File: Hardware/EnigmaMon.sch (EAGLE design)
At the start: 57 parts, among them IC1 4051N, IC2 TLC5940, IC3 MEGA8-P, T1 BC548, T2 BC548, T3 BC548, T4 BC548, T5 BC548, T6 BC548, T8 BC548, T9 BC548

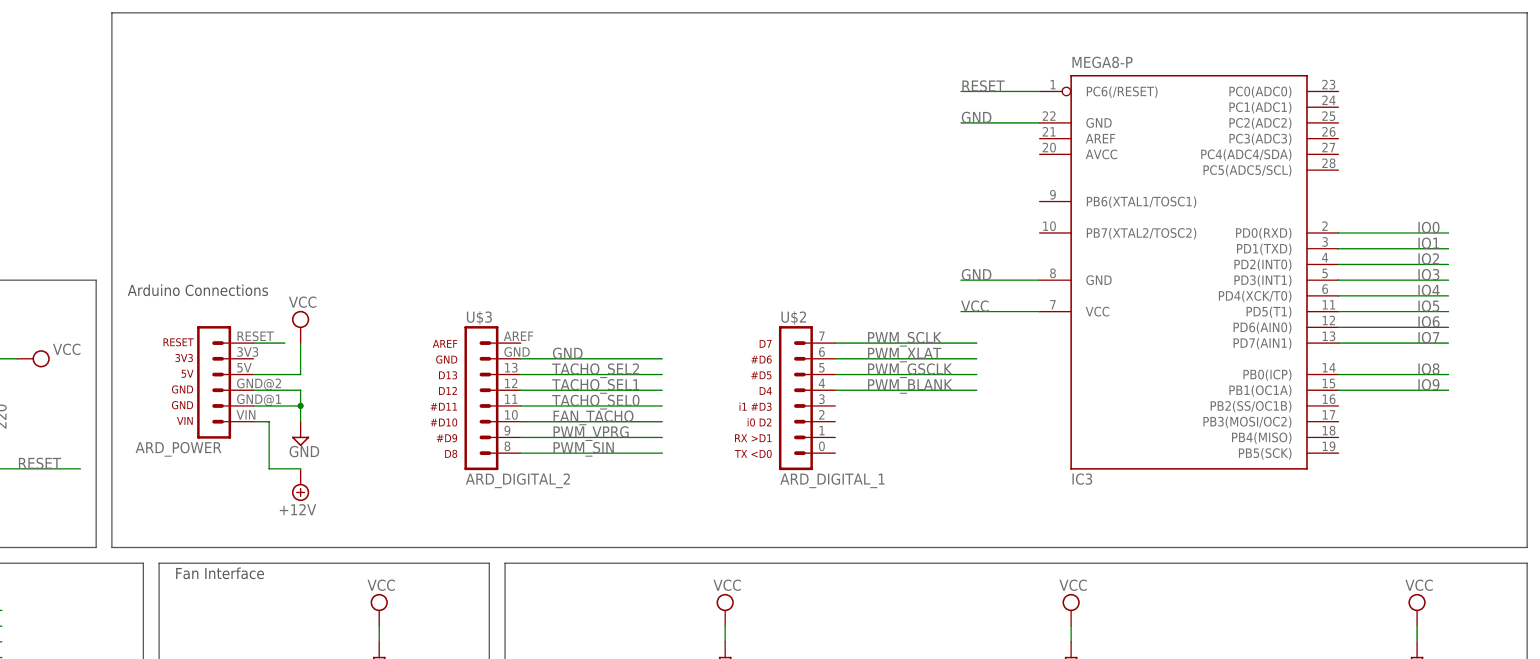
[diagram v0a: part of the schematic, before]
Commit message: Started wiring for on-board ATmega
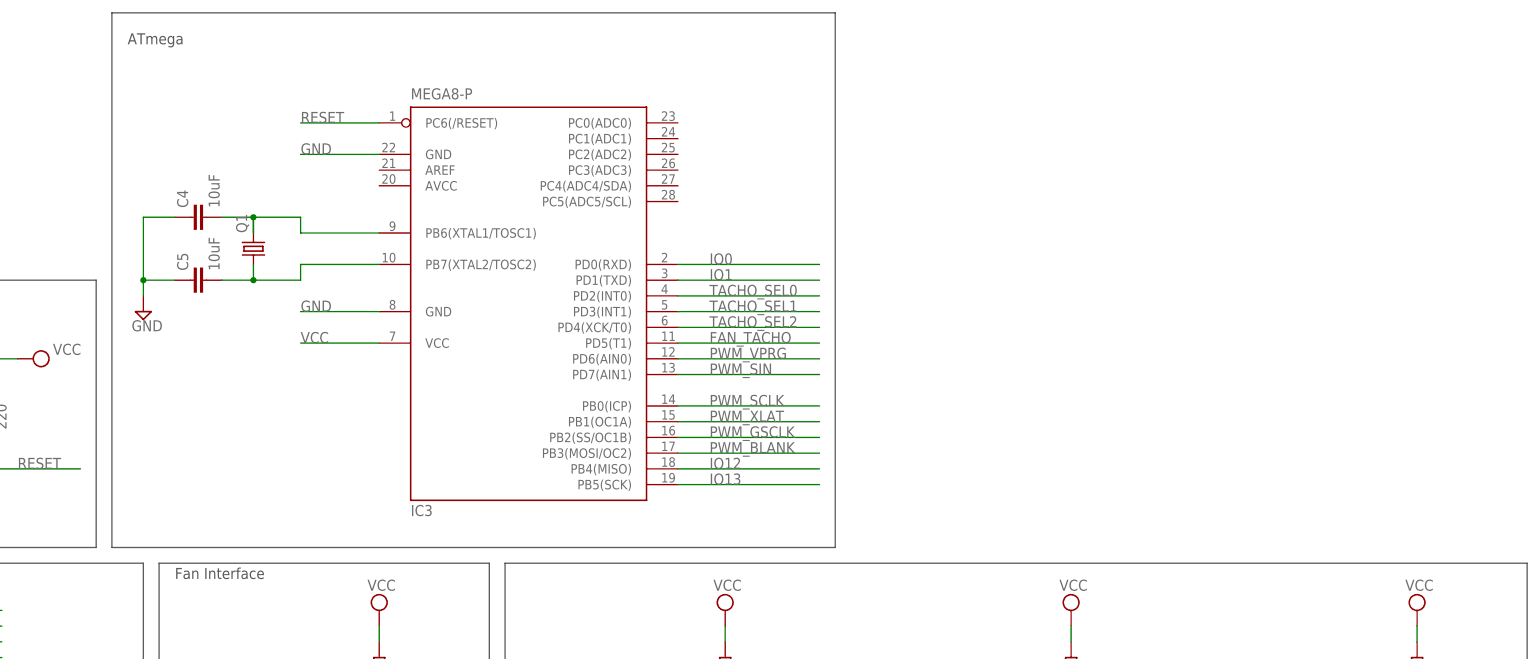
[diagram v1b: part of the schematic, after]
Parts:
- removed U$1: ARD_POWER, EnigmaMon:ARD_POWER
- removed U$2: ARD_DIGITAL_1, EnigmaMon:ARD_DIGITAL_1
- removed U$3: ARD_DIGITAL_2, EnigmaMon:ARD_DIGITAL_2
- added C4, C5: 10uF, rcl:C-EU025-025X050
- added Q1: (no value), EnigmaMon:CRYSTALHC49S
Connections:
- removed net IO2: IC3.PD2(INT0)
- removed net IO3: IC3.PD3(INT1)
- removed net IO4: IC3.PD4(XCK/T0)
- removed net IO5: IC3.PD5(T1)
- removed net IO6: IC3.PD6(AIN0)
- removed net IO7: IC3.PD7(AIN1)
- removed net IO8: IC3.PB0(ICP)
- removed net IO9: IC3.PB1(OC1A)
- new net IO12: IC3.PB4(MISO)
- new net IO13: IC3.PB5(SCK)
- new net N$11: C4.2, IC3.PB6(XTAL1/TOSC1), Q1.2
- new net N$12: C5.2, IC3.PB7(XTAL2/TOSC2), Q1.1
- net +12V: no longer U$1.VIN
- net FAN_TACHO: now also IC3.PD5(T1); no longer U$3.10
- net GND: now also C4.1, C5.1; no longer U$1.GND@1, U$1.GND@2, U$3.GND
- net PWM_BLANK: now also IC3.PB3(MOSI/OC2); no longer U$2.4
- net PWM_GSCLK: now also IC3.PB2(SS/OC1B); no longer U$2.5
- net PWM_SCLK: now also IC3.PB0(ICP); no longer U$2.7
- net PWM_SIN: now also IC3.PD7(AIN1); no longer U$3.8
- net PWM_VPRG: now also IC3.PD6(AIN0); no longer U$3.9
- net PWM_XLAT: now also IC3.PB1(OC1A); no longer U$2.6
- net RESET: no longer U$1.RESET
- net TACHO_SEL0: now also IC3.PD2(INT0); no longer U$3.11
- net TACHO_SEL1: now also IC3.PD3(INT1); no longer U$3.12
- net TACHO_SEL2: now also IC3.PD4(XCK/T0); no longer U$3.13
- net VCC: no longer U$1.5V
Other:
- note added: "ATmega"
- note removed: "Arduino Connections"
- moved on the sheet: IC3

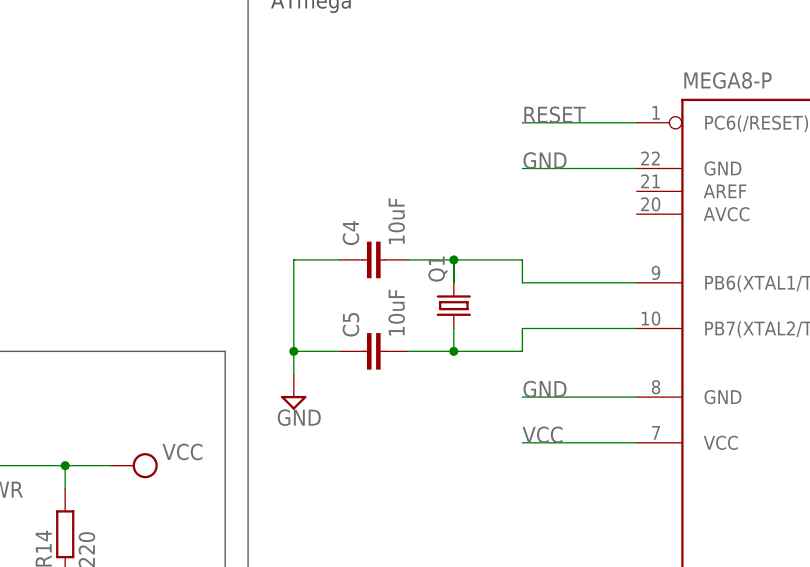
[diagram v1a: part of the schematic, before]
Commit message: Added test for the fan tacho
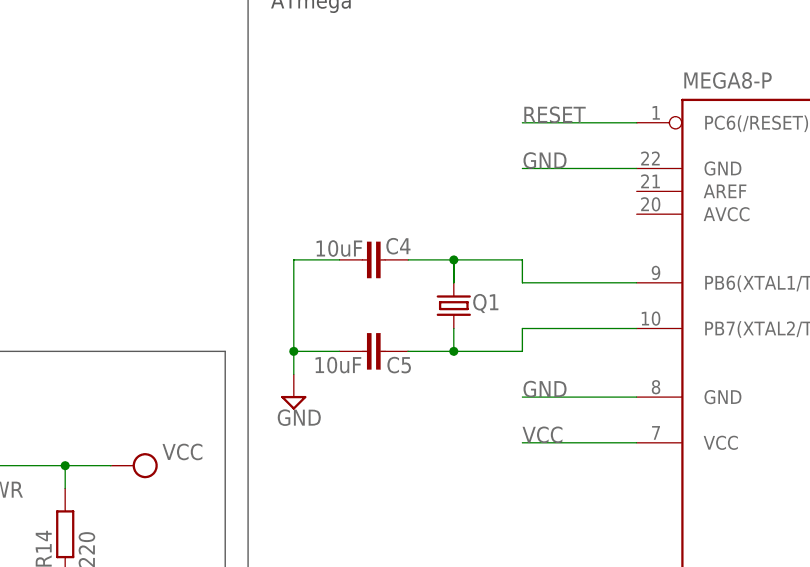
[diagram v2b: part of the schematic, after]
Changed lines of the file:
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@@
 <instance part="SUPPLY10" gate="GND" x="78.74" y="17.78"/>
 <instance part="IC3" gate="G$1" x="160.02" y="185.42"/>
-<instance part="Q1" gate="G$1" x="116.84" y="193.04" rot="R90"/>
-<instance part="C4" gate="G$1" x="106.68" y="198.12" rot="R90"/>
-<instance part="C5" gate="G$1" x="106.68" y="187.96" rot="R90"/>
+<instance part="Q1" gate="G$1" x="116.84" y="193.04" smashed="yes" rot="R90">
+<attribute name="NAME" x="118.872" y="192.532" size="1.778" layer="95"/>
+<attribute name="VALUE" x="119.38" y="195.58" size="1.778" layer="96" rot="R90"/>
+</instance>
+<instance part="C4" gate="G$1" x="106.68" y="198.12" smashed="yes" rot="R90">
+<attribute name="NAME" x="109.22" y="198.755" size="1.778" layer="95"/>
+<attribute name="VALUE" x="101.346" y="198.501" size="1.778" layer="96"/>
+</instance>
+<instance part="C5" gate="G$1" x="106.68" y="187.96" smashed="yes" rot="R90">
+<attribute name="NAME" x="112.268" y="187.325" size="1.778" layer="95" rot="R180"/>
+<attribute name="VALUE" x="106.68" y="187.325" size="1.778" layer="96" rot="R180"/>
+</instance>
 <instance part="SUPPLY2" gate="GND" x="99.06" y="182.88"/>
 </instances>

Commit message: Testing
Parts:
- D1, D2, D3, D4, D5, D6, D8, D9: value 1N4004 -> (none); device diode:1N4004 -> diode:DIODE-D-5
- FAN1, FAN2, FAN3, FAN4, FAN5, FAN6, FAN7, FAN8: value (none) -> FAN; device pinhead:PINHD-1X3 -> EnigmaMon:FAN
- R1, R4: device rcl:R-EU_0207/10 -> rcl:R-EU_0204/5
- R10, R11, R12, R15, R16, R17, R18, R2, R3, R5, R6, R7, R8, R9: device rcl:R-EU_0204/7 -> rcl:R-EU_0204/5
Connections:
- removed net FAN1_GND: D1.C, FAN1.3, T1.C
- removed net FAN2_GND: D2.C, FAN2.3, T2.C
- removed net FAN3_GND: D3.C, FAN3.3, T3.C
- removed net FAN4_GND: D4.C, FAN4.3, T4.C
- removed net FAN5_GND: D5.C, FAN5.3, T5.C
- removed net FAN6_GND: D6.C, FAN6.3, T6.C
- removed net FAN7_GND: D8.C, FAN7.3, T8.C
- removed net FAN8_GND: D9.C, FAN8.3, T9.C
- new net N$13: D2.A, FAN2.GND, T2.C
- new net N$14: D3.A, FAN3.GND, T3.C
- new net N$15: D4.A, FAN4.GND, T4.C
- new net N$16: D1.A, FAN1.GND, T1.C
- new net N$17: D9.A, FAN8.GND, T9.C
- new net N$19: D8.A, FAN7.GND, T8.C
- new net N$20: D6.A, FAN6.GND, T6.C
- new net N$21: D5.A, FAN5.GND, T5.C
- net +12V: now also D1.C, D2.C, D3.C, D4.C, D5.C, D6.C, D8.C, D9.C, FAN1.VCC, FAN2.VCC, FAN3.VCC, FAN4.VCC, FAN5.VCC, FAN6.VCC, FAN7.VCC, FAN8.VCC; no longer FAN1.2, FAN2.2, FAN3.2, FAN4.2, FAN5.2, FAN6.2, FAN7.2, FAN8.2
- net FAN1_TACHO: now also FAN1.TACHO; no longer FAN1.1
- net FAN2_TACHO: now also FAN2.TACHO; no longer FAN2.1
- net FAN3_TACHO: now also FAN3.TACHO; no longer FAN3.1
- net FAN4_TACHO: now also FAN4.TACHO; no longer FAN4.1
- net FAN5_TACHO: now also FAN5.TACHO; no longer FAN5.1
- net FAN6_TACHO: now also FAN6.TACHO; no longer FAN6.1
- net FAN7_TACHO: now also FAN7.TACHO; no longer FAN7.1
- net FAN8_TACHO: now also FAN8.TACHO; no longer FAN8.1
- net GND: no longer D1.A, D2.A, D3.A, D4.A, D5.A, D6.A, D8.A, D9.A
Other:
- moved on the sheet: R1, R10, R12, R16, R18, R4, R6, R8
